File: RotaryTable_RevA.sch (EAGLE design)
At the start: 85 parts, among them CON1 USB_BMULTICOMP, CON2 ICSP, CON4 CON_5X2, CON5 CON_5X100MIL, CON6 CON_4X200MIL, IC1 PIC18F26J50SO28, IC2 LD1117, IC3 24AA16, IC4 74AHCT125, IC5 74HC14D, IC6 LMT86, IC7 ULN2003, IC8 MCP16311, SW1 PEC11R, SW2 PEC11R, SW3 PEC09, SW4 PEC09, X1 ABM3-8.000MHZ-D2Y-T, X2 BUZZER

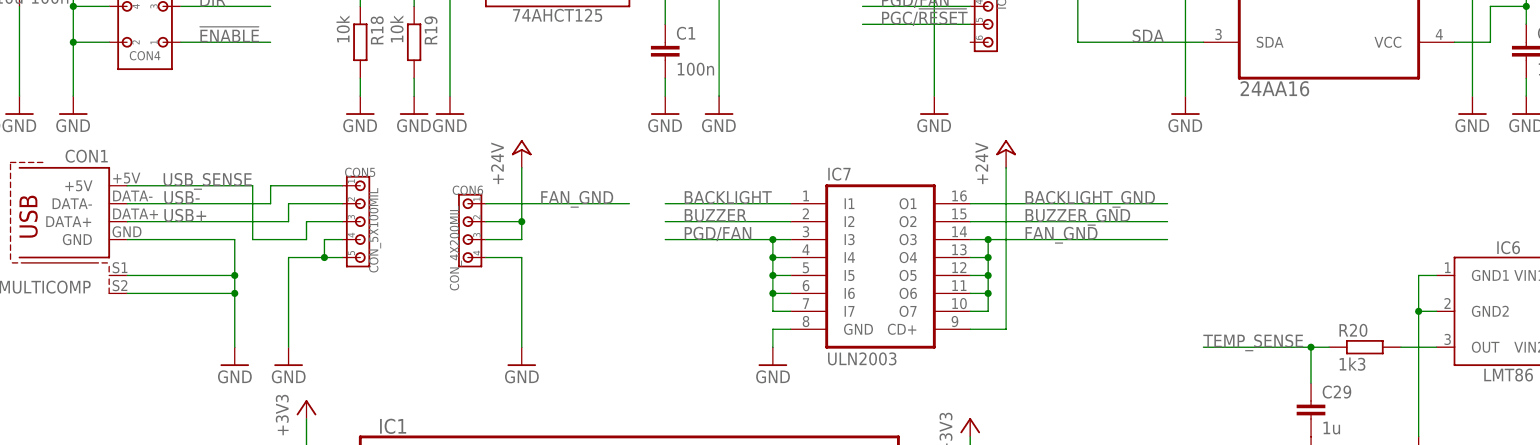
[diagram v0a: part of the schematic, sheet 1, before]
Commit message: USB header changed, header for external temperature sensor added, some ground vias added
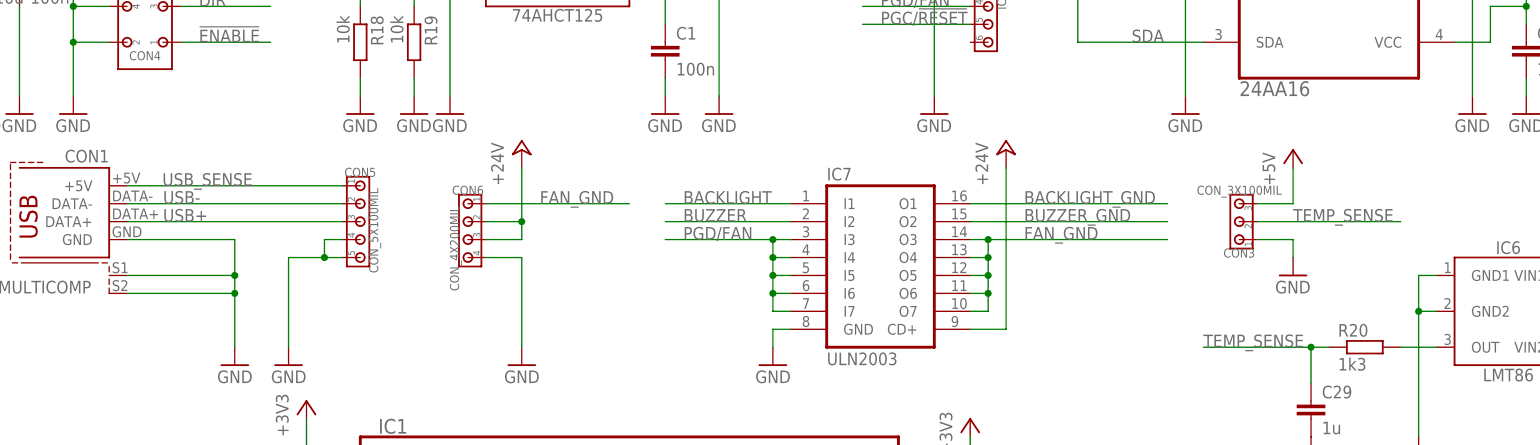
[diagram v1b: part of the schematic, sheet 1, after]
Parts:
- added CON3: CON_3X100MIL, 00Connector:CON_3X100MIL
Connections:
- net +5V: now also CON3.3
- net GND: now also CON3.1
- net TEMP_SENSE: now also CON3.2
- net USB+: now also CON5.3; no longer CON5.2
- net USB-: now also CON5.2; no longer CON5.1
- net USB_SENSE: now also CON5.1; no longer CON5.3
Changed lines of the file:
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@@
 <part name="R25" library="00Resistor" deviceset="RESISTOR" device="R0805" value="220"/>
 <part name="CON6" library="00Connector" deviceset="CON_4X" device="200MIL"/>
+<part name="CON3" library="00Connector" deviceset="CON_3X" device="100MIL"/>
+<part name="P+10" library="00Supply" deviceset="+5V" device=""/>
+<part name="GND68" library="00Supply" deviceset="GND" device=""/>
 </parts>
 <sheets>
@@
 <instance part="GND67" gate="1" x="7.62" y="124.46"/>
 <instance part="CON6" gate="G$1" x="76.2" y="111.76" rot="MR270"/>
+<instance part="CON3" gate="G$1" x="185.42" y="109.22" rot="R90"/>
+<instance part="P+10" gate="1" x="193.04" y="119.38"/>
+<instance part="GND68" gate="1" x="193.04" y="101.6"/>
 </instances>
 <busses>
@@
 <wire x1="12.7" y1="127" x2="12.7" y2="139.7" width="0.1524" layer="91"/>
 </segment>
+<segment>
+<pinref part="CON3" gate="G$1" pin="1"/>
+<pinref part="GND68" gate="1" pin="GND"/>
+<wire x1="187.96" y1="106.68" x2="193.04" y2="106.68" width="0.1524" layer="91"/>
+<wire x1="193.04" y1="106.68" x2="193.04" y2="104.14" width="0.1524" layer="91"/>
+</segment>
 </net>
 <net name="PGD/FAN" class="0">
@@
 <segment>
 <pinref part="CON1" gate="G$1" pin="DATA+"/>
-<wire x1="27.94" y1="109.22" x2="50.8" y2="109.22" width="0.1524" layer="91"/>
+<wire x1="27.94" y1="109.22" x2="58.42" y2="109.22" width="0.1524" layer="91"/>
 <label x="33.02" y="109.22" size="1.778" layer="95"/>
-<wire x1="50.8" y1="109.22" x2="50.8" y2="111.76" width="0.1524" layer="91"/>
-<pinref part="CON5" gate="G$1" pin="2"/>
-<wire x1="50.8" y1="111.76" x2="58.42" y2="111.76" width="0.1524" layer="91"/>
+<pinref part="CON5" gate="G$1" pin="3"/>
 </segment>
 <segment>
@@
 <segment>
 <pinref part="CON1" gate="G$1" pin="DATA-"/>
-<wire x1="27.94" y1="111.76" x2="48.26" y2="111.76" width="0.1524" layer="91"/>
+<wire x1="27.94" y1="111.76" x2="58.42" y2="111.76" width="0.1524" layer="91"/>
 <label x="33.02" y="111.76" size="1.778" layer="95"/>
-<wire x1="48.26" y1="111.76" x2="48.26" y2="114.3" width="0.1524" layer="91"/>
-<pinref part="CON5" gate="G$1" pin="1"/>
-<wire x1="48.26" y1="114.3" x2="58.42" y2="114.3" width="0.1524" layer="91"/>
+<pinref part="CON5" gate="G$1" pin="2"/>
 </segment>
 <segment>
@@
 <segment>
 <pinref part="CON1" gate="G$1" pin="+5V"/>
-<wire x1="27.94" y1="114.3" x2="45.72" y2="114.3" width="0.1524" layer="91"/>
+<wire x1="27.94" y1="114.3" x2="58.42" y2="114.3" width="0.1524" layer="91"/>
 <label x="45.72" y="114.3" size="1.778" layer="95" rot="MR0"/>
-<wire x1="45.72" y1="114.3" x2="45.72" y2="106.68" width="0.1524" layer="91"/>
-<wire x1="45.72" y1="106.68" x2="53.34" y2="106.68" width="0.1524" layer="91"/>
-<wire x1="53.34" y1="106.68" x2="53.34" y2="109.22" width="0.1524" layer="91"/>
-<pinref part="CON5" gate="G$1" pin="3"/>
-<wire x1="53.34" y1="109.22" x2="58.42" y2="109.22" width="0.1524" layer="91"/>
+<pinref part="CON5" gate="G$1" pin="1"/>
 </segment>
 <segment>
@@
 <wire x1="203.2" y1="55.88" x2="200.66" y2="55.88" width="0.1524" layer="91"/>
 <junction x="200.66" y="55.88"/>
+</segment>
+<segment>
+<pinref part="CON3" gate="G$1" pin="3"/>
+<pinref part="P+10" gate="1" pin="+5V"/>
+<wire x1="187.96" y1="111.76" x2="193.04" y2="111.76" width="0.1524" layer="91"/>
+<wire x1="193.04" y1="111.76" x2="193.04" y2="116.84" width="0.1524" layer="91"/>
 </segment>
 </net>
@@
 <label x="33.02" y="71.12" size="1.778" layer="95"/>
 </segment>
-</net>
+<segment>
+<pinref part="CON3" gate="G$1" pin="2"/>
+<wire x1="187.96" y1="109.22" x2="208.28" y2="109.22" width="0.1524" layer="91"/>
+<label x="193.04" y="109.22" size="1.778" layer="95"/>
+</segment>
+</net>

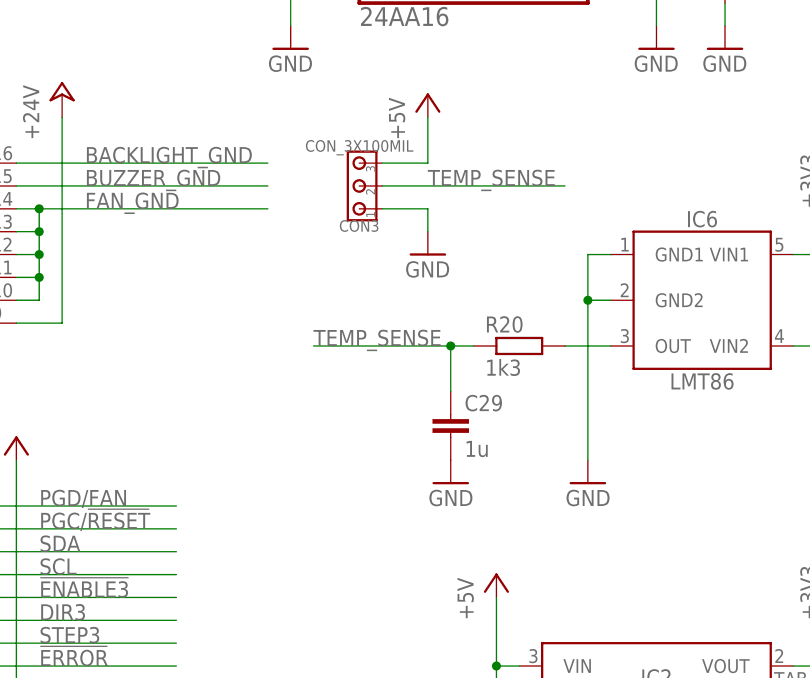
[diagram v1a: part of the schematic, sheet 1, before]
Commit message: Bug related to external temperature sensing fixed
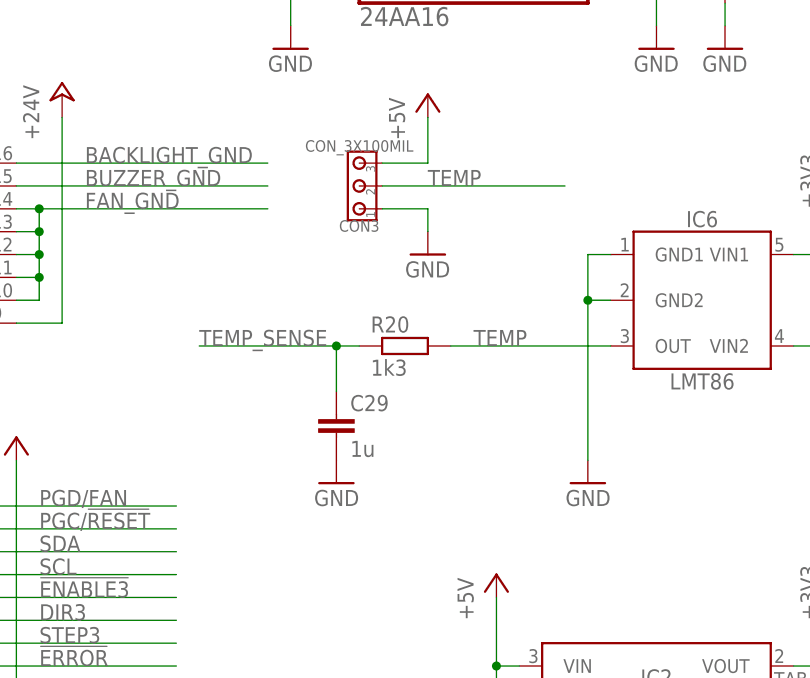
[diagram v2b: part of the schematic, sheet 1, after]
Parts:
- L1: value (none) -> 22u
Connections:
- removed net N$2: IC6.OUT, R20.2
- new net TEMP: CON3.2, IC6.OUT, R20.2
- net TEMP_SENSE: no longer CON3.2
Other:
- moved on the sheet: C29, R20
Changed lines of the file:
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@@
 <part name="GND60" library="00Supply" deviceset="GND" device=""/>
 <part name="GND61" library="00Supply" deviceset="GND" device=""/>
-<part name="L1" library="00Inductor" deviceset="INDUCTOR" device="SRN5040"/>
+<part name="L1" library="00Inductor" deviceset="INDUCTOR" device="SRN5040" value="22u"/>
 <part name="GND62" library="00Supply" deviceset="GND" device=""/>
 <part name="GND63" library="00Supply" deviceset="GND" device=""/>
@@
 <instance part="IC6" gate="G$1" x="223.52" y="96.52"/>
 <instance part="C28" gate="G$1" x="238.76" y="83.82"/>
-<instance part="C29" gate="G$1" x="195.58" y="83.82"/>
-<instance part="R20" gate="G$1" x="203.2" y="91.44"/>
-<instance part="GND54" gate="1" x="195.58" y="76.2" rot="MR0"/>
+<instance part="C29" gate="G$1" x="182.88" y="83.82"/>
+<instance part="R20" gate="G$1" x="190.5" y="91.44"/>
+<instance part="GND54" gate="1" x="182.88" y="76.2" rot="MR0"/>
 <instance part="GND55" gate="1" x="238.76" y="76.2" rot="MR0"/>
 <instance part="GND56" gate="1" x="210.82" y="76.2" rot="MR0"/>
@@
 </segment>
 </net>
-<net name="N$2" class="0">
+<net name="TEMP" class="0">
 <segment>
 <pinref part="IC6" gate="G$1" pin="OUT"/>
 <pinref part="R20" gate="G$1" pin="2"/>
-<wire x1="208.28" y1="91.44" x2="213.36" y2="91.44" width="0.1524" layer="91"/>
+<wire x1="195.58" y1="91.44" x2="213.36" y2="91.44" width="0.1524" layer="91"/>
+<label x="198.12" y="91.44" size="1.778" layer="95"/>
+</segment>
+<segment>
+<pinref part="CON3" gate="G$1" pin="2"/>
+<wire x1="187.96" y1="109.22" x2="208.28" y2="109.22" width="0.1524" layer="91"/>
+<label x="193.04" y="109.22" size="1.778" layer="95"/>
 </segment>
 </net>
@@
 <segment>
 <pinref part="R20" gate="G$1" pin="1"/>
-<wire x1="198.12" y1="91.44" x2="195.58" y2="91.44" width="0.1524" layer="91"/>
+<wire x1="185.42" y1="91.44" x2="182.88" y2="91.44" width="0.1524" layer="91"/>
 <pinref part="C29" gate="G$1" pin="1"/>
-<wire x1="195.58" y1="91.44" x2="180.34" y2="91.44" width="0.1524" layer="91"/>
-<wire x1="195.58" y1="86.36" x2="195.58" y2="91.44" width="0.1524" layer="91"/>
-<junction x="195.58" y="91.44"/>
-<label x="180.34" y="91.44" size="1.778" layer="95"/>
+<wire x1="182.88" y1="91.44" x2="167.64" y2="91.44" width="0.1524" layer="91"/>
+<wire x1="182.88" y1="86.36" x2="182.88" y2="91.44" width="0.1524" layer="91"/>
+<junction x="182.88" y="91.44"/>
+<label x="167.64" y="91.44" size="1.778" layer="95"/>
 </segment>
 <segment>
@@
 <label x="33.02" y="71.12" size="1.778" layer="95"/>
 </segment>
-<segment>
-<pinref part="CON3" gate="G$1" pin="2"/>
-<wire x1="187.96" y1="109.22" x2="208.28" y2="109.22" width="0.1524" layer="91"/>
-<label x="193.04" y="109.22" size="1.778" layer="95"/>
-</segment>
-</net>
+</net>

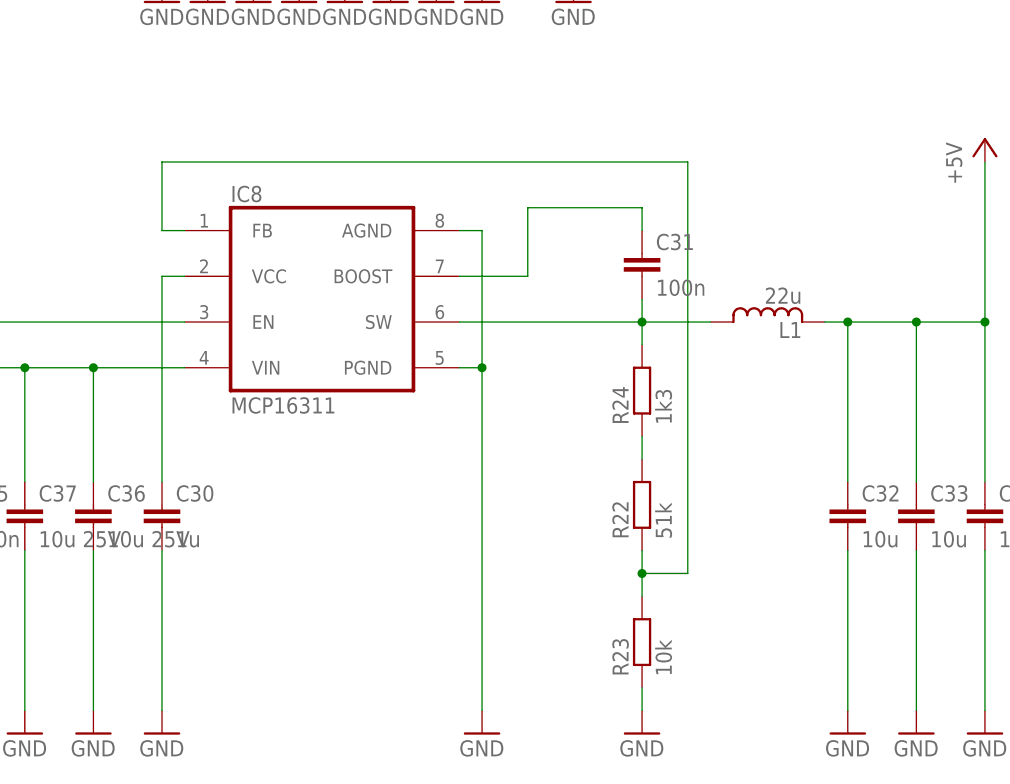
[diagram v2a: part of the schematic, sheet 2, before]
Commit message: Error in schematic and in board layout fixed. Voltage regulator feedback was taken from the wrong side of the coil.
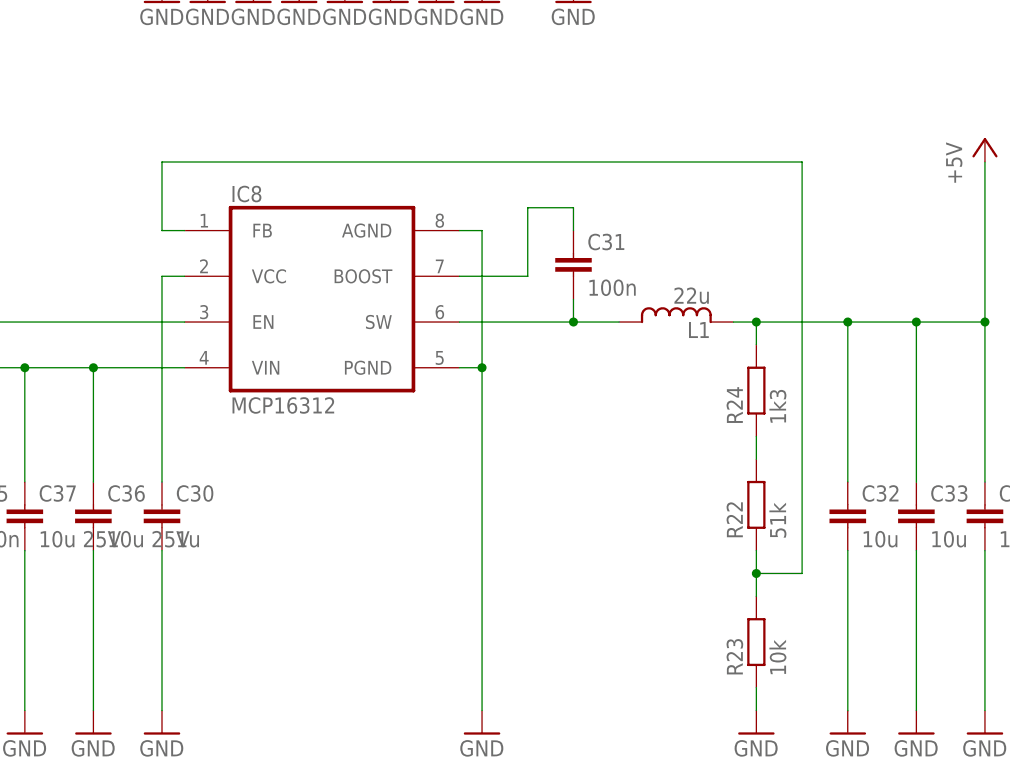
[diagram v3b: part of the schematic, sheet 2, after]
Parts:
- IC7: value ULN2003 -> TPL7407
- IC8: value MCP16311 -> MCP16312
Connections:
- removed net N$16: C31.2, IC8.SW, L1.1, R24.2
- new net N$2: C31.2, IC8.SW, L1.1
- net +5V: now also R24.2
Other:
- moved on the sheet: C31, L1, R22, R23, R24
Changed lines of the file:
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@@
 <part name="P+5" library="supply1" deviceset="+24V" device=""/>
 <part name="GND53" library="00Supply" deviceset="GND" device=""/>
-<part name="IC7" library="00Transistor" deviceset="ULN2003" device=""/>
+<part name="IC7" library="00Transistor" deviceset="ULN2003" device="" value="TPL7407"/>
 <part name="IC6" library="00Sensor" deviceset="LMT86" device=""/>
 <part name="C28" library="00Capacitor" deviceset="C" device="C0805" value="100n"/>
@@
 <part name="R21" library="00Resistor" deviceset="RESISTOR" device="R0805" value="10k"/>
 <part name="P+6" library="supply1" deviceset="+24V" device=""/>
-<part name="IC8" library="00VoltageRegulator" deviceset="MCP16311" device=""/>
+<part name="IC8" library="00VoltageRegulator" deviceset="MCP16311" device="" value="MCP16312"/>
 <part name="C30" library="00Capacitor" deviceset="C" device="C0805" value="1u"/>
 <part name="GND57" library="00Supply" deviceset="GND" device=""/>
@@
 <instance part="P+7" gate="1" x="129.54" y="93.98"/>
 <instance part="GND58" gate="1" x="137.16" y="27.94"/>
-<instance part="C31" gate="G$1" x="205.74" y="81.28"/>
+<instance part="C31" gate="G$1" x="198.12" y="81.28"/>
 <instance part="GND59" gate="1" x="187.96" y="27.94"/>
 <instance part="C32" gate="G$1" x="228.6" y="53.34"/>
@@
 <instance part="GND60" gate="1" x="129.54" y="27.94"/>
 <instance part="GND61" gate="1" x="144.78" y="27.94"/>
-<instance part="L1" gate="G$1" x="218.44" y="73.66"/>
+<instance part="L1" gate="G$1" x="208.28" y="73.66"/>
 <instance part="GND62" gate="1" x="228.6" y="27.94"/>
 <instance part="GND63" gate="1" x="236.22" y="27.94"/>
@@
 <instance part="+3V16" gate="G$1" x="104.14" y="60.96"/>
 <instance part="P+8" gate="1" x="243.84" y="93.98"/>
-<instance part="R22" gate="G$1" x="205.74" y="53.34" rot="R90"/>
-<instance part="R23" gate="G$1" x="205.74" y="38.1" rot="R90"/>
-<instance part="GND65" gate="1" x="205.74" y="27.94"/>
-<instance part="R24" gate="G$1" x="205.74" y="66.04" rot="R90"/>
+<instance part="R22" gate="G$1" x="218.44" y="53.34" rot="R90"/>
+<instance part="R23" gate="G$1" x="218.44" y="38.1" rot="R90"/>
+<instance part="GND65" gate="1" x="218.44" y="27.94"/>
+<instance part="R24" gate="G$1" x="218.44" y="66.04" rot="R90"/>
 <instance part="P+9" gate="1" x="228.6" y="170.18"/>
 <instance part="R25" gate="G$1" x="228.6" y="160.02" rot="R90"/>
@@
 <pinref part="GND65" gate="1" pin="GND"/>
 <pinref part="R23" gate="G$1" pin="1"/>
-<wire x1="205.74" y1="33.02" x2="205.74" y2="30.48" width="0.1524" layer="91"/>
+<wire x1="218.44" y1="33.02" x2="218.44" y2="30.48" width="0.1524" layer="91"/>
 </segment>
 </net>
@@
 <wire x1="193.04" y1="78.74" x2="193.04" y2="86.36" width="0.1524" layer="91"/>
 <pinref part="C31" gate="G$1" pin="1"/>
-<wire x1="193.04" y1="86.36" x2="205.74" y2="86.36" width="0.1524" layer="91"/>
-<wire x1="205.74" y1="86.36" x2="205.74" y2="83.82" width="0.1524" layer="91"/>
+<wire x1="193.04" y1="86.36" x2="198.12" y2="86.36" width="0.1524" layer="91"/>
+<wire x1="198.12" y1="86.36" x2="198.12" y2="83.82" width="0.1524" layer="91"/>
 </segment>
 </net>
@@
 <segment>
 <pinref part="L1" gate="G$1" pin="2"/>
-<wire x1="226.06" y1="73.66" x2="228.6" y2="73.66" width="0.1524" layer="91"/>
+<wire x1="215.9" y1="73.66" x2="218.44" y2="73.66" width="0.1524" layer="91"/>
 <pinref part="C32" gate="G$1" pin="1"/>
+<wire x1="218.44" y1="73.66" x2="228.6" y2="73.66" width="0.1524" layer="91"/>
 <wire x1="228.6" y1="73.66" x2="236.22" y2="73.66" width="0.1524" layer="91"/>
 <wire x1="236.22" y1="73.66" x2="243.84" y2="73.66" width="0.1524" layer="91"/>
@@
 <junction x="243.84" y="73.66"/>
 <pinref part="P+8" gate="1" pin="+5V"/>
+<pinref part="R24" gate="G$1" pin="2"/>
+<wire x1="218.44" y1="71.12" x2="218.44" y2="73.66" width="0.1524" layer="91"/>
+<junction x="218.44" y="73.66"/>
 </segment>
 <segment>
@@
 <pinref part="R22" gate="G$1" pin="1"/>
 <pinref part="R23" gate="G$1" pin="2"/>
-<wire x1="205.74" y1="43.18" x2="205.74" y2="45.72" width="0.1524" layer="91"/>
-<wire x1="205.74" y1="45.72" x2="205.74" y2="48.26" width="0.1524" layer="91"/>
-<wire x1="205.74" y1="45.72" x2="210.82" y2="45.72" width="0.1524" layer="91"/>
+<wire x1="218.44" y1="43.18" x2="218.44" y2="45.72" width="0.1524" layer="91"/>
+<wire x1="218.44" y1="45.72" x2="218.44" y2="48.26" width="0.1524" layer="91"/>
+<wire x1="218.44" y1="45.72" x2="223.52" y2="45.72" width="0.1524" layer="91"/>
 <pinref part="IC8" gate="G$1" pin="FB"/>
 <wire x1="154.94" y1="83.82" x2="152.4" y2="83.82" width="0.1524" layer="91"/>
 <wire x1="152.4" y1="83.82" x2="152.4" y2="91.44" width="0.1524" layer="91"/>
-<wire x1="152.4" y1="91.44" x2="210.82" y2="91.44" width="0.1524" layer="91"/>
-<wire x1="210.82" y1="45.72" x2="210.82" y2="91.44" width="0.1524" layer="91"/>
-<junction x="205.74" y="45.72"/>
-</segment>
-</net>
-<net name="N$16" class="0">
-<segment>
-<pinref part="L1" gate="G$1" pin="1"/>
-<pinref part="C31" gate="G$1" pin="2"/>
-<wire x1="205.74" y1="73.66" x2="205.74" y2="76.2" width="0.1524" layer="91"/>
-<wire x1="205.74" y1="73.66" x2="213.36" y2="73.66" width="0.1524" layer="91"/>
-<junction x="205.74" y="73.66"/>
-<pinref part="IC8" gate="G$1" pin="SW"/>
-<wire x1="185.42" y1="73.66" x2="205.74" y2="73.66" width="0.1524" layer="91"/>
-<pinref part="R24" gate="G$1" pin="2"/>
-<wire x1="205.74" y1="73.66" x2="205.74" y2="71.12" width="0.1524" layer="91"/>
+<wire x1="152.4" y1="91.44" x2="223.52" y2="91.44" width="0.1524" layer="91"/>
+<wire x1="223.52" y1="45.72" x2="223.52" y2="91.44" width="0.1524" layer="91"/>
+<junction x="218.44" y="45.72"/>
 </segment>
 </net>
@@
 <pinref part="R22" gate="G$1" pin="2"/>
 <pinref part="R24" gate="G$1" pin="1"/>
-<wire x1="205.74" y1="60.96" x2="205.74" y2="58.42" width="0.1524" layer="91"/>
+<wire x1="218.44" y1="60.96" x2="218.44" y2="58.42" width="0.1524" layer="91"/>
 </segment>
 </net>
@@
 </segment>
 </net>
+<net name="N$2" class="0">
+<segment>
+<pinref part="IC8" gate="G$1" pin="SW"/>
+<pinref part="L1" gate="G$1" pin="1"/>
+<wire x1="185.42" y1="73.66" x2="198.12" y2="73.66" width="0.1524" layer="91"/>
+<pinref part="C31" gate="G$1" pin="2"/>
+<wire x1="198.12" y1="73.66" x2="203.2" y2="73.66" width="0.1524" layer="91"/>
+<wire x1="198.12" y1="76.2" x2="198.12" y2="73.66" width="0.1524" layer="91"/>
+<junction x="198.12" y="73.66"/>
+</segment>
+</net>
